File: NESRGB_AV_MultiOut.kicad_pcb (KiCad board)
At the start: 16 copper layers, 22.2 x 20.4 mm, 14 parts

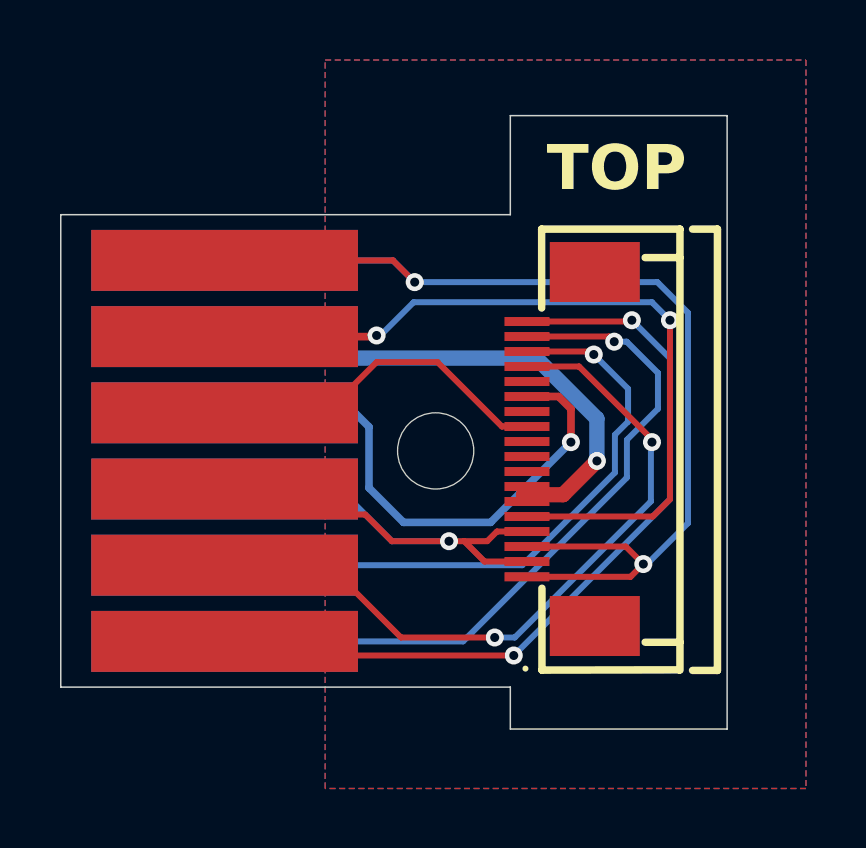
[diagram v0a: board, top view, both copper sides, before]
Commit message: Create scripts for github ci and for creating fabrication outputs.
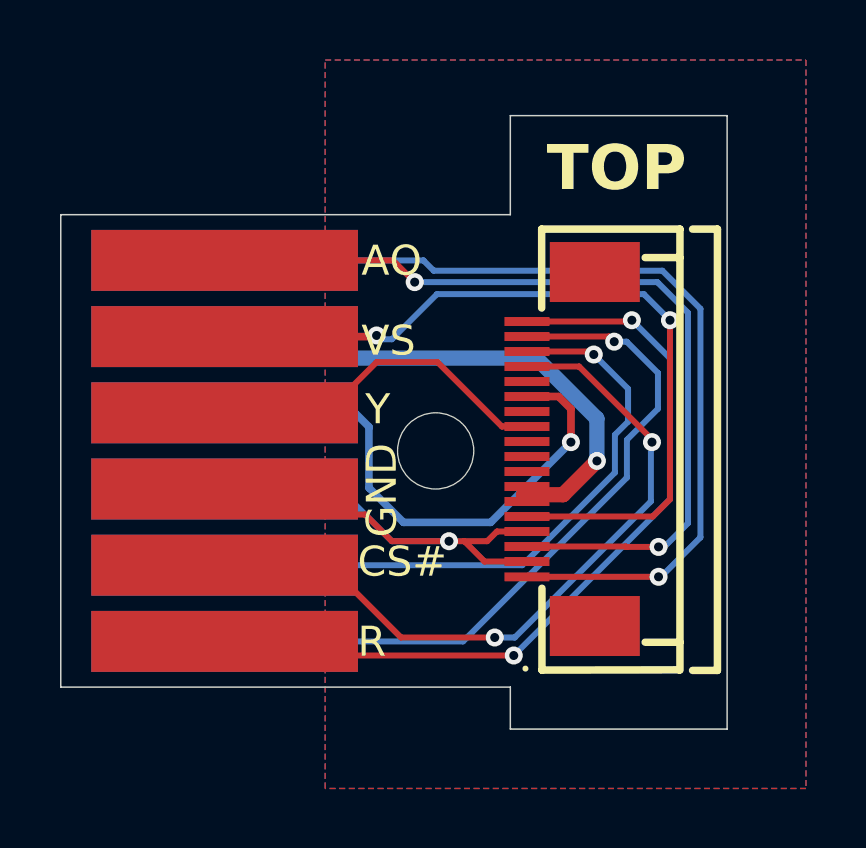
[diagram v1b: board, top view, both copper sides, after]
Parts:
- PAD1, PAD10, PAD11, PAD12, PAD2, PAD3, PAD4, PAD5, PAD6, PAD7, PAD8, PAD9: value (none) -> SMD_PADNIN_AV
- X1: renamed from REF**; value C262640_FPC-SMD_AFC07-S18ECA-00 -> AFC07-S18ECA-00
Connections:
- net +5V renamed /+5V
- net BLUE renamed /BLUE
- net C renamed /C
- net CSYNC renamed /CSYNC
- net CVBS renamed /CVBS
- net GND renamed /GND
- net GREEN renamed /GREEN
- net MONO_AUD renamed /MONO_AUD
- net RED renamed /RED
- net Y renamed /Y
- X1 pad 19: (no net) -> unconnected-(X1-Pad19)
- X1 pad 20: (no net) -> unconnected-(X1-Pad20)
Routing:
- net /MONO_AUD: track 40.0 -> 59.4 mm, vias 2 -> 3
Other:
- board text added: "+5V"
- board text added: "AO"
- board text added: "B"
- board text added: "BOTTOM"
- board text added: "C"
- board text added: "CS#"
- board text added: "G"
- board text added: "GND"
- board text added: "NESRGB FFC Multiout Original Design zaxour X FragolTech For NESRGB v5 and Up Juvinious"
- board text added: "R"
- board text added: "VS"
- board text added: "Y"
- board text removed: "NESRGB Multiout zaxour X FragolTech"

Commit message: Added checks for erc/drc in github ci. Added badges to README. Cleaned up all erc/drc, all clean.
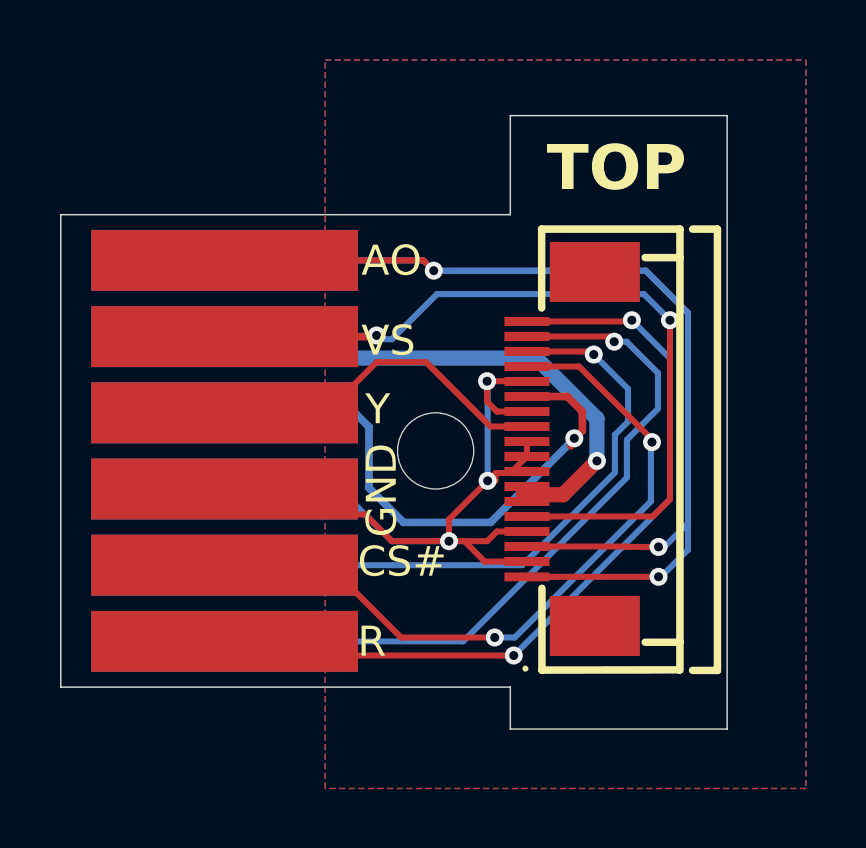
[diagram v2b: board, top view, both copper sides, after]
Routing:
- net /GND: track 21.6 -> 33.2 mm, vias 1 -> 3
- net /C: track 19.1 -> 19.8 mm
- net /MONO_AUD: track 59.4 -> 58.7 mm
